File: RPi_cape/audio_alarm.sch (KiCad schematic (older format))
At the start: 59 parts, among them J13 Conn_01x02, J14 Conn_01x02, Q5 MMBT3904, Q6 MMBT3904, Q7 MMBT3904, Q8 MMBT3904, U17 LM2903, U24 TL431A, U25 LM2903, U26 MIC1557, U27 MIC1557, U28 LM4871M

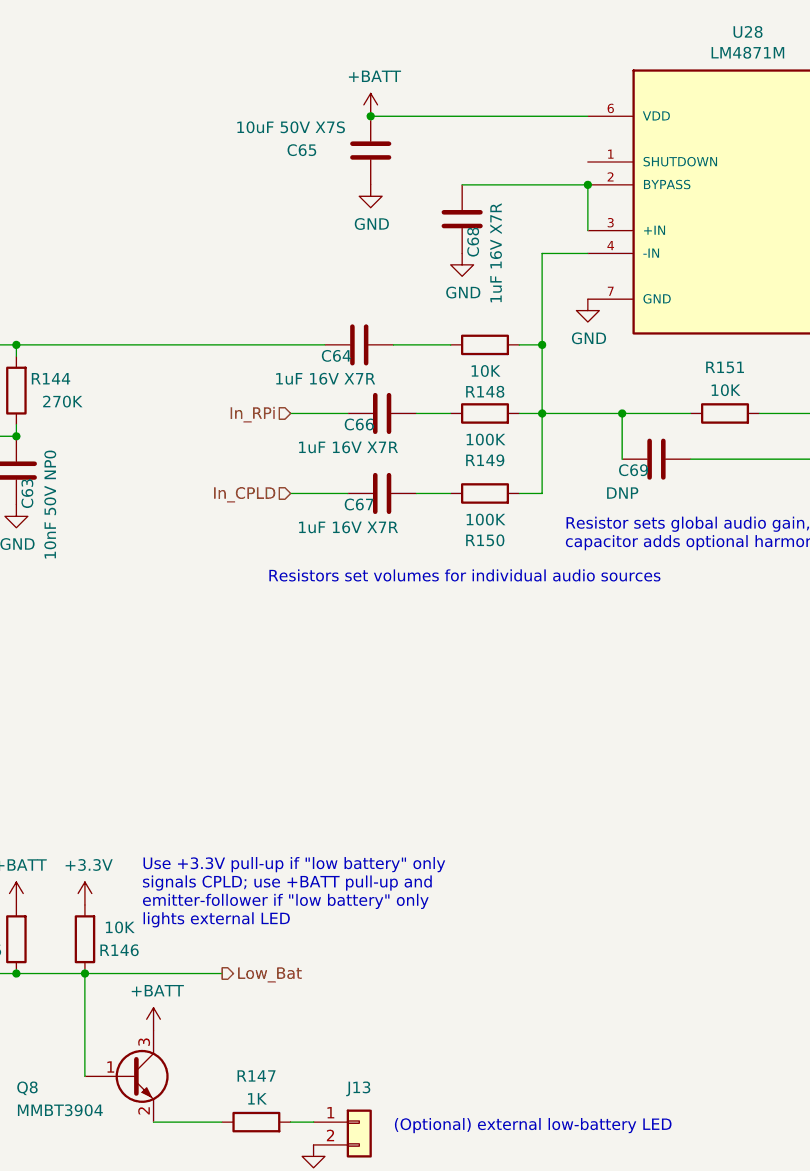
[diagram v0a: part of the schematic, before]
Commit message: Extra info, post-design-review fixes
Added extra info on existing alternate circuit options
Added extra info on parts selection
Created initial PCB file
Added bulk cap to +5V input
Design review fixes:
Moved Raspberry Pi PWM output to GPIO18 to take advantage of hardware PWM
Fixed floating shutdown input on audio amp
Added series resistor R177 to allow low battery output to signal to both CPLD and external LED at the same time
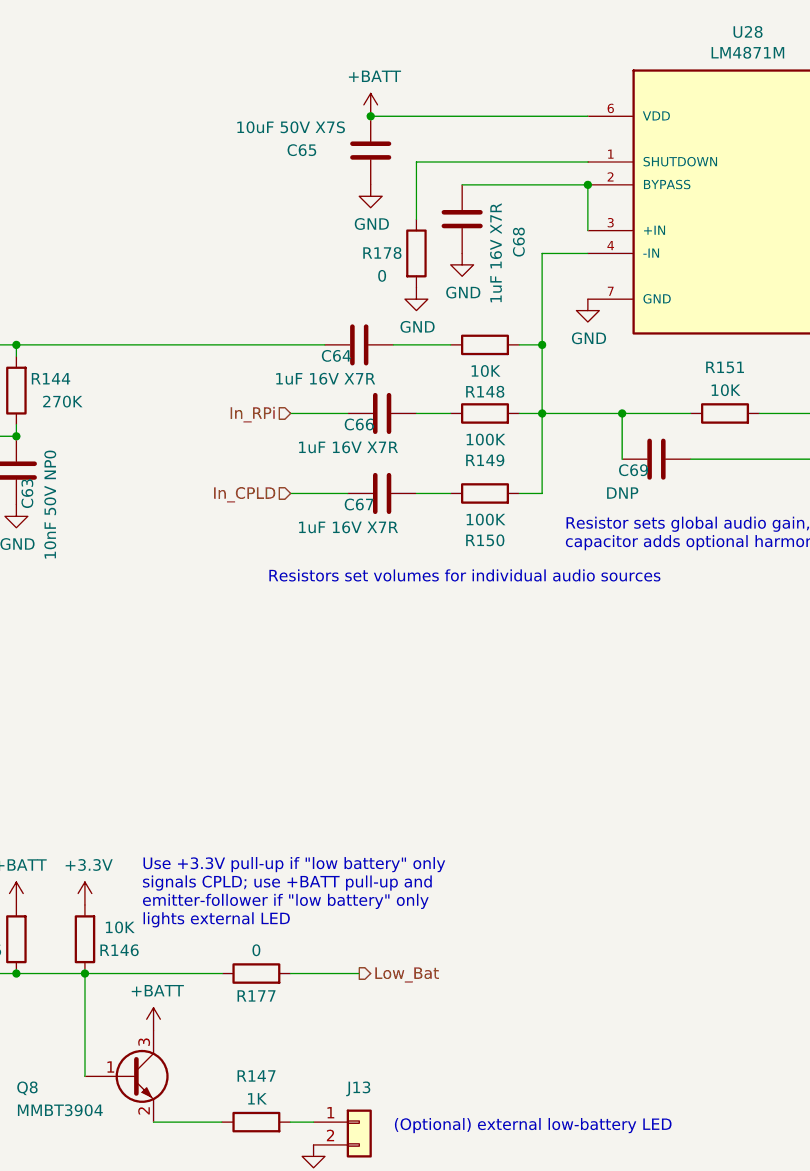
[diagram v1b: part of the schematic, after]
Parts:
- added R177, R178: 0, Resistor_SMD:R_1206_3216Metric, symbol Device:R
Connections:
- net GND: now also R178.2
- net Low_Bat: now also R177.2; no longer Q8.1 (B), R143.1, R145.1, R146.1, U25.7
- net at U28.1 (SHUTDOWN): now also R178.1
- new net: Q8.1 (B), R143.1, R145.1, R146.1, R177.1, U25.7
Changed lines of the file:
@@
 Title "Audible Alarm"
 Date ""
-Rev "1.0"
+Rev "1.1"
 Comp "Partners COVID Innovation Group"
 Comment1 "Don Straney"
@@
 AR Path="/5E8A4ABF/5F16700F" Ref="C?"  Part="1"
 AR Path="/5E8E1F08/5F16700F" Ref="C68"  Part="1"
-F 0 "C68" V 8050 1900 50  0000 C CNN
+F 0 "C68" V 7850 1900 50  0000 C CNN
 F 1 "1uF 16V X7R" V 7950 1950 50  0000 C CNN
 F 2 "Capacitor_SMD:C_0805_2012Metric" H 8138 1650 50  0001 C CNN
@@
 Wire Wire Line
 	6450 5100 7050 5100
-Text HLabel 7050 5100 2    50   Output ~ 0
+Text HLabel 7650 5100 2    50   Output ~ 0
 Low_Bat
 Wire Wire Line
@@
 Text Notes 6700 4900 0    50   ~ 0
 Use +3.3V pull-up if "low battery" only\nsignals CPLD; use +BATT pull-up and\nemitter-follower if "low battery" only\nlights external LED
+$Comp
+L Device:R R?
+U 1 1 5E98635F
+P 7200 5100
+AR Path="/5E98635F" Ref="R?"  Part="1"
+AR Path="/5E8AFE9D/5E98635F" Ref="R?"  Part="1"
+AR Path="/5E8A4ABF/5E98635F" Ref="R?"  Part="1"
+AR Path="/5E8E1F08/5E98635F" Ref="R177"  Part="1"
+F 0 "R177" V 7100 5100 50  0000 C CNN
+F 1 "0" V 7300 5100 50  0000 C CNN
+F 2 "Resistor_SMD:R_1206_3216Metric" V 7130 5100 50  0001 C CNN
+F 3 "~" H 7200 5100 50  0001 C CNN
+	1    7200 5100
+	0    -1   -1   0
+$EndComp
+Wire Wire Line
+	7350 5100 7650 5100
+$Comp
+L Device:R R?
+U 1 1 5E9EE857
+P 7900 1950
+AR Path="/5E9EE857" Ref="R?"  Part="1"
+AR Path="/5E8AFE9D/5E9EE857" Ref="R?"  Part="1"
+AR Path="/5E8A4ABF/5E9EE857" Ref="R?"  Part="1"
+AR Path="/5E8E1F08/5E9EE857" Ref="R178"  Part="1"
+F 0 "R178" H 7750 1950 50  0000 C CNN
+F 1 "0" H 7750 1850 50  0000 C CNN
+F 2 "Resistor_SMD:R_1206_3216Metric" V 7830 1950 50  0001 C CNN
+F 3 "~" H 7900 1950 50  0001 C CNN
+	1    7900 1950
+	1    0    0    -1
+$EndComp
+$Comp
+L power:GND #PWR?
+U 1 1 5E9EFF41
+P 7900 2100
+AR Path="/5E9EFF41" Ref="#PWR?"  Part="1"
+AR Path="/5E8AFE9D/5E9EFF41" Ref="#PWR?"  Part="1"
+AR Path="/5E8A4ABF/5E9EFF41" Ref="#PWR?"  Part="1"
+AR Path="/5E8E1F08/5E9EFF41" Ref="#PWR0319"  Part="1"
+F 0 "#PWR0319" H 7900 1850 50  0001 C CNN
+F 1 "GND" H 7905 1927 50  0000 C CNN
+F 2 "" H 7900 2100 50  0001 C CNN
+F 3 "" H 7900 2100 50  0001 C CNN
+	1    7900 2100
+	1    0    0    -1
+$EndComp
+Wire Wire Line
+	7900 1800 7900 1550
+Wire Wire Line
+	7900 1550 8650 1550
 $EndSCHEMATC

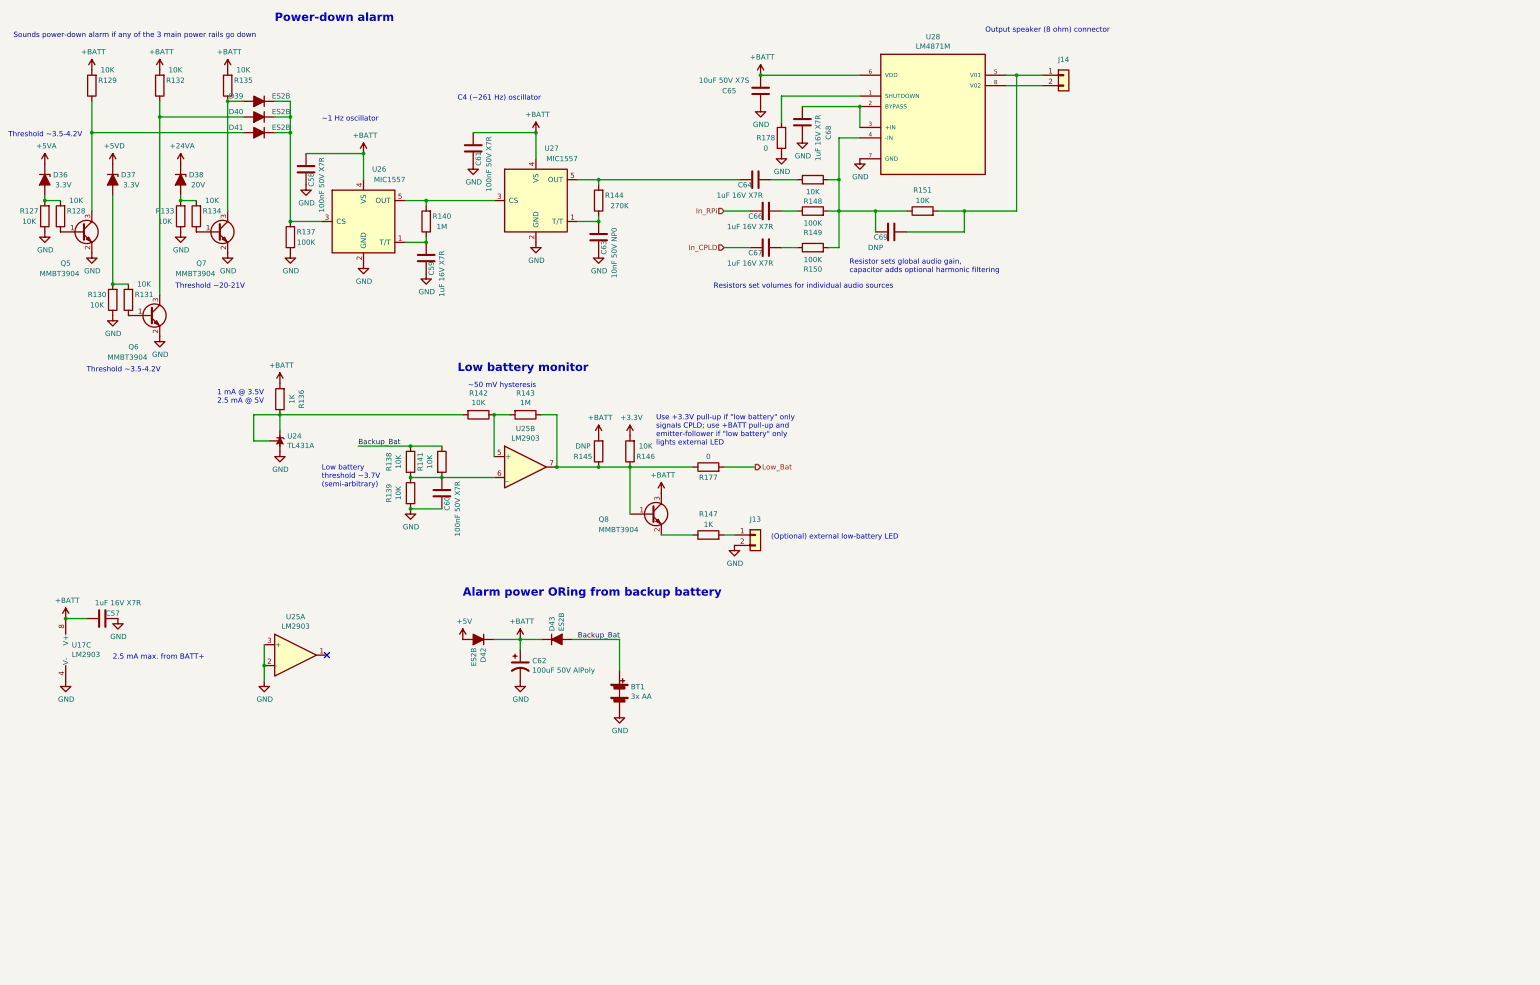
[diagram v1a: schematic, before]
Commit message: Finished schematic, most of PCB placement
Added error budget for analog inputs
Finished most of PCB placement and started routing
Added R185, R186 to allow powering CPLD from alarm power for better power-down alarm sound flexibility
Changed power-down alarm monitoring from +5VD to +3.3V, and put +5VA and +24VA monitoring as DNP by default, to match the CPLD's ability to run off backup battery and monitor +5VA/+24VA
Moved from 3x AA (4.5V) to 4x AA (6V) alarm battery for better audio voltage, and added PNP diode-ORing circuit (Q12 etc.) to accomodate higher voltage, changed low-battery threshold to 5V
Added pull-down resistors to sensor op-amp outputs to help extend low-end output range
Changed 1nF, 10nF, 100nF caps to 0603-size for better fit of CPLD decoupling caps
Added additional bulk cap C19 to audio amp's supply just in case of alarm-induced supply fluctuations
Decreased CPLD's I2C pull-up values to deal with anticipated PCB capacitance etc.
Removed additional dual-op-amp footprint option on analog inputs, due to high availability of single op-amps
Adjusted O2 sensor input clamping to reduce errors from diode leakage current (changed from zener to low-leakage clamps to rails)
Changed O2 sensor op-amp to different lower-offset part to reduce total error from +/- 4.2% FS to +/- 1.7% FS
Fixed missing power section for U17
Added rotary encoder input
Consolidated +5VA fuse options
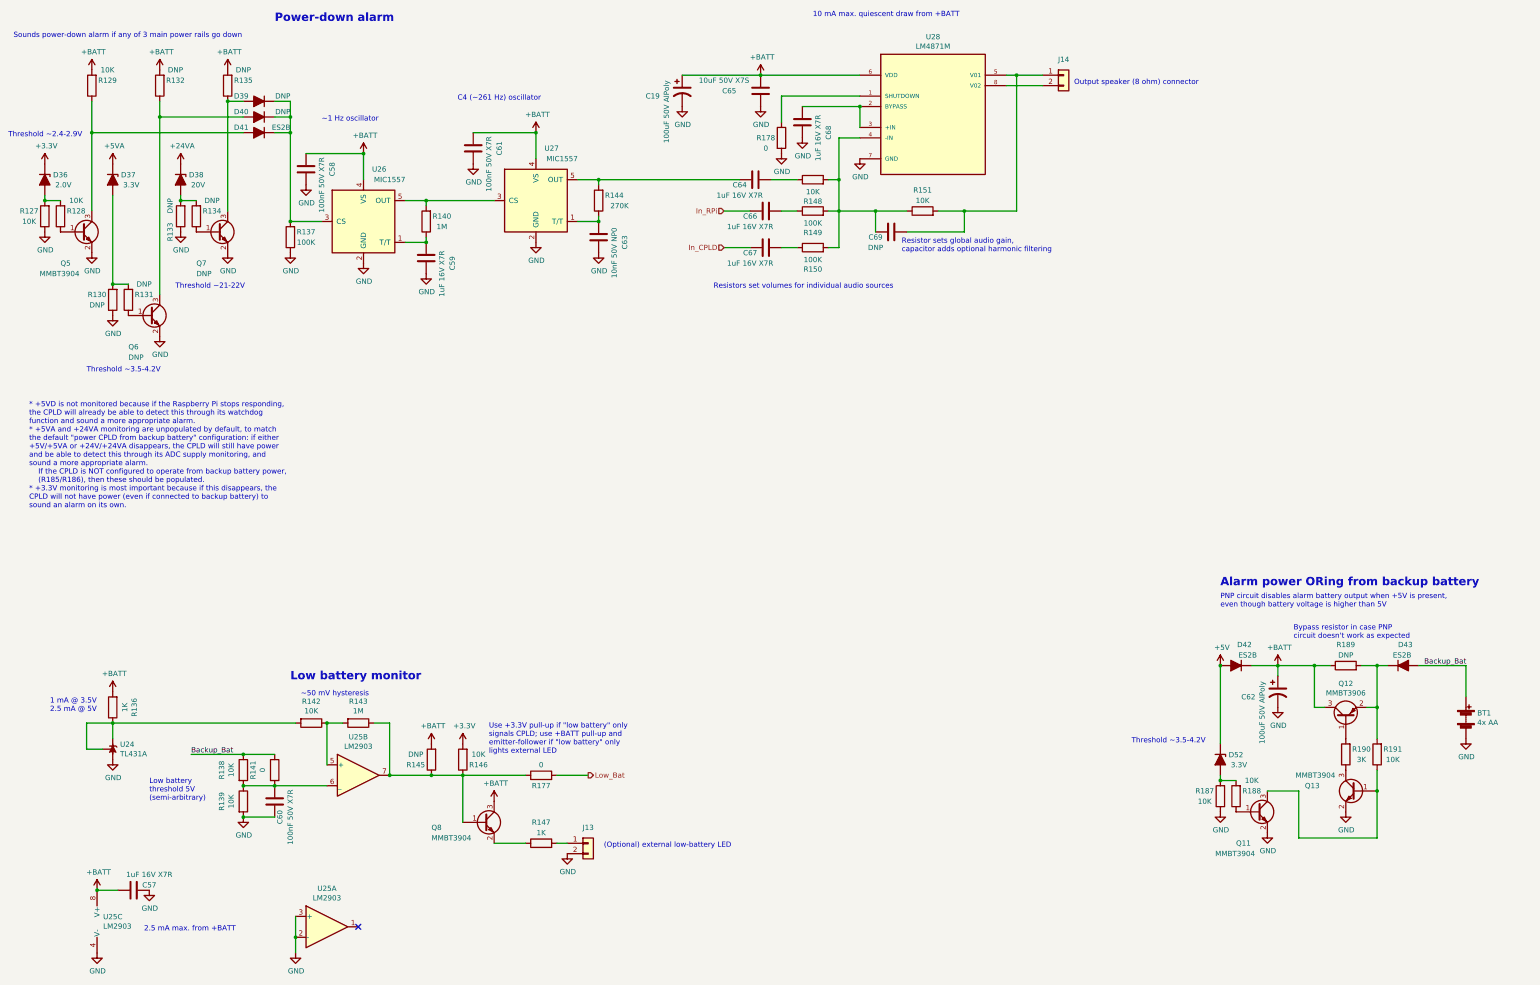
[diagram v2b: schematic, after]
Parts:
- removed U17: LM2903, Package_SO:VSSOP-8_3.0x3.0mm_P0.65mm, symbol Comparator:LM2903
- added C19: 100uF 50V AlPoly, Capacitor_SMD:CP_Elec_10x10.5, symbol Device:CP1
- added D52: 3.3V, Diode_SMD:D_SOD-123, symbol Device:D_Zener_ALT
- added Q11, Q13: MMBT3904, Package_TO_SOT_SMD:SOT-23, symbol Transistor_BJT:MMBT3904
- added Q12: MMBT3906, Package_TO_SOT_SMD:SOT-23, symbol Transistor_BJT:MMBT3906
- added R187, R188, R191: 10K, Resistor_SMD:R_1206_3216Metric, symbol Device:R
- added R189: DNP, Resistor_SMD:R_1206_3216Metric, symbol Device:R
- added R190: 3K, Resistor_SMD:R_1206_3216Metric, symbol Device:R
- added unit 3 of U25
- BT1: value 3x AA -> 4x AA
- C58, C60, C61: footprint Capacitor_SMD:C_0805_2012Metric -> Capacitor_SMD:C_0603_1608Metric; Part Number 08055C104KAT2A -> 06035C104JAT2A
- C63: footprint Capacitor_SMD:C_0805_2012Metric -> Capacitor_SMD:C_0603_1608Metric; Manufacturer Samsung -> Murata; Part Number CL21C103JBFNNNG -> GRM1885C1H103JA01D
- D36: value 3.3V -> 2.0V
- D39, D40: value ES2B -> DNP
- Q6, Q7: value MMBT3904 -> DNP
- R130, R131, R132, R133, R134, R135: value 10K -> DNP
- R141: value 10K -> 0
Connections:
- net +5VD is gone; now on net +5VA: D37.1 (K)
- net +3V3: now also D36.1 (K)
- net +5V: now also D52.1 (K)
- net +5VA: no longer D36.1 (K)
- net +BATT: now also C19.1, Q12.3 (C), R189.1, U25.8 (V+); no longer D43.1 (K)
- net GND: now also C19.2, Q11.2 (E), Q13.2 (E), R187.1, U25.4 (V-)
- new net: D52.2 (A), R187.2, R188.2
- new net: Q11.1 (B), R188.1
- new net: Q11.3 (C), Q13.1 (B), R191.1
- new net: Q12.1 (B), R190.2
- new net: D43.1 (K), Q12.2 (E), R189.2, R191.2
- new net: Q13.3 (C), R190.1
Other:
- note added: "* +5VD is not monitored because if the Raspberry Pi stops responding,\nthe CPLD will already be able to detect this through its watchdog\nfunction and sound a more appropriate alarm.\n* +5VA and +24VA monitoring are unpopulated by default, to match\nthe default "power CPLD from backup battery" configuration: if either\n+5V/+5VA or +24V/+24VA disappears, the CPLD will still have power\nand be able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"
- note added: "10 mA max. quiescent draw from +BATT"
- note added: "2.5 mA max. from +BATT"
- note added: "Bypass resistor in case PNP\ncircuit doesn't work as expected"
- note added: "Low battery\nthreshold 5V\n(semi-arbitrary)"
- note added: "PNP circuit disables alarm battery output when +5V is present,\neven though battery voltage is higher than 5V"
- note added: "Sounds power-down alarm if any of 3 main power rails go down"
- note added: "Threshold ~~2.4-2.9V"
- note added: "Threshold ~~21-22V"
- note removed: "2.5 mA max. from BATT+"
- note removed: "Low battery\nthreshold ~~3.7V\n(semi-arbitrary)"
- note removed: "Sounds power-down alarm if any of the 3 main power rails go down"
- note removed: "Threshold ~~20-21V"
- moved on the sheet: BT1, C57, C60, C62, D42, D43, J13, Q8, R136, R138, R139, R141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
